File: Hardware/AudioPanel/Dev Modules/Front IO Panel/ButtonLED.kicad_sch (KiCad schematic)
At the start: 6 parts, among them U19 WS2811

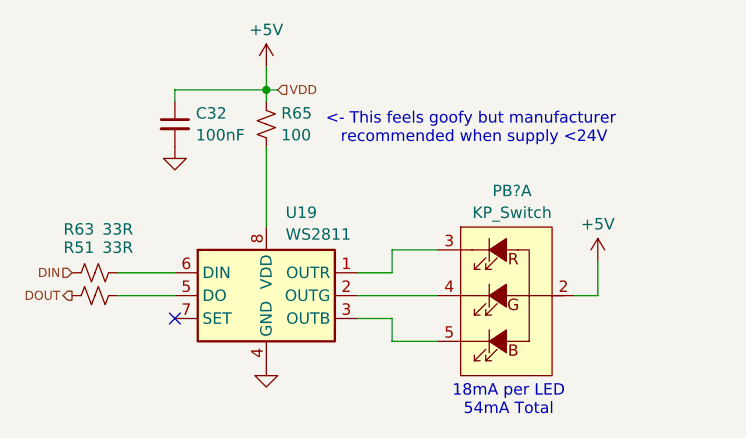
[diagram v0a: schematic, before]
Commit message: Adding LEDs
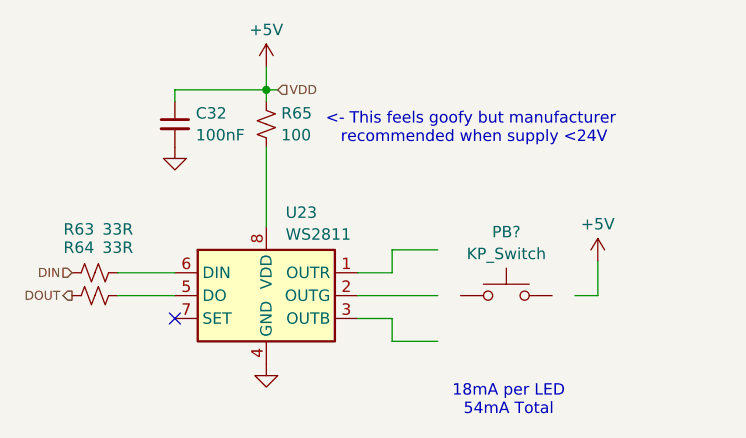
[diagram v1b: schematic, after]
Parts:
- PB?: symbol AudioPanelLibrary:KP_Switch -> Switch:SW_Push
- renumbered R51 to R64, U19 to U23
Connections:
- net +5V: no longer PB?.2 (A)
- net at U23.1 (OUTR): no longer PB?.3 (K_R)
- net at U23.2 (OUTG): no longer PB?.4 (K_G)
- net at U23.3 (OUTB): no longer PB?.5 (K_B)
